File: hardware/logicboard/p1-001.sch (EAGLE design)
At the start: 70 parts, among them IC1 74LS06N, IC2 4066N, J1 MKR, J2 GPIO, J3 Vcc, J4 RLY, J42 RLY2, J5 SPI, J6 LED, J7 DIN5, J8 DIN5, J9 DIN5, K1 G5V1, Q1 220mA/50V/3.5Ω, Q2 220mA/50V/3.5Ω, T1 2SC1815, U1 DS18B20

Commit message: Removed many parts.
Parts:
- removed A, B: (no value), wirepad:SMD2
- removed C1: 22u, rcl:C-EU025-050X050
- removed C11, C4: 100n, rcl:C-EU025-024X044
- removed C12, C13, C3: 1u, rcl:C-EU050-024X044
- removed C2: 470n, rcl:C-EU050-024X044
- removed D1: DIODE-1N4148, SparkFun-DiscreteSemi:DIODE-1N4148
- removed F1: 1.8A, fuse:TE5
- removed H1, H2: STAND-OFF, SparkFun-Hardware:STAND-OFF
- removed IC1: 74LS06N, 74xx-us:74LS06N
- removed IC2: 4066N, 40xx:4066N
- removed J1: MKR, SparkFun-Connectors:CONN_05JST
- removed J2: GPIO, SparkFun-Connectors:CONN_03JST-PTH
- removed J3: Vcc, SparkFun-Connectors:CONN_02JST-PTH-2
- removed J4: RLY, SparkFun-Connectors:CONN_02-JST-2MM-SMT
- removed J5: SPI, SparkFun-Connectors:CONN_05JST-VERT
- removed J8, J9: DIN5, SparkFun-Connectors:DIN5
- removed JP1: PWRSEL, pinhead:PINHD-2X3
- removed JP2: RTC, SparkFun-Connectors:CONN_05
- removed JP4: RLYJMP, pinhead:PINHD-1X2
- removed JP5: PWR, pinhead:PINHD-1X3
- removed JP7: MNTR, pinhead:PINHD-1X4
- removed LCD1: AQM0802A-RN-GBW, AQM0802A-RN-GBW:AQM0802A-RN-GBW
- removed Q1, Q2: 220mA/50V/3.5Ω, SparkFun-DiscreteSemi:MOSFET-NCH-BSS138
- removed R101, R102, R103, R104: 10k, rcl:R-EU_M2012
- removed RN1: 10k, resistor-net:RN04
- removed RZ1**, RZ2**, VCCBRIDGE**: Inf, rcl:R-EU_M2012
- removed SV1: (no value), con-ml:ML16LE
- removed U1: DS18B20, SparkFun-Sensors:DS18B20
- removed V1: 5V, v-reg:78XXL
- removed VDDBRIDGE: 0, rcl:R-EU_M2012
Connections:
- removed net ANLG0R: IC2A.B, SV1-3.S
- removed net ANLG1R: IC2B.B, SV1-7.S
- removed net ANLG2R: IC2C.B, SV1-11.S
- removed net ANLG3R: IC2D.B, SV1-15.S
- removed net CAP1N: C12.2, LCD1.3
- removed net CAP1P: C12.1, LCD1.4
- removed net LCDVOUT: C13.2, LCD1.2
- removed net MO2RTN: RN4H.2
- removed net MO2SND: RN4G.2
- removed net MORTN: J9.5, RN4D.2
- removed net MOSND: J9.4, RN4C.2
- removed net MTRTN: J8.5, RN4F.2
- removed net MTSND: J8.4, RN4E.2
- removed net N$1: IC1D.O, RN4F.1
- removed net N$2: IC1E.O, RN4D.1
- removed net N$6: IC1F.O, RN4H.1
- removed net RLYOUT: J4.1, J42.1, K12.S
- removed net SCL: J1.3, Q1.D, R101.1, RZ1**.1
- removed net SDA3V: LCD1.7, Q2.S, R104.1, RZ2**.2
- removed net V+: C1.1, C2.1, D1.C, J0.3, JP1.1, JP5.3, V1.IN
- removed net VCC/VDD: C11.1, C13.1, LCD1.5, LCD1.9, VCCBRIDGE**.1, VDDBRIDGE.1
- removed net VOUT: F1.2, JP1.4, JP1.6
- removed net VOUTRAW: B.P, C3.1, C4.1, D1.A, J4.2, J42.2, JP4.2, K12.P, K12.P@1, V1.OUT
- removed net VOUTRAW2: A.P, F1.1, JP4.1, K12.O
- new net RLYOUT1: J42.1, K12.S
- new net RLYOUT2: J42.2, K12.P, K12.P@1
- net ANLG0: no longer IC2A.A, RN1.2
- net ANLG1: no longer IC2B.A, RN1.3
- net ANLG2: no longer IC2C.A, RN1.4
- net ANLG3: no longer IC2D.A, RN1.5
- net D7GATE: no longer IC2A.C, IC2B.C, IC2C.C, IC2D.C, J1.4
- net DTCT0: no longer SV1-2.S
- net DTCT1: no longer SV1-6.S
- net DTCT2: no longer SV1-10.S
- net DTCT3: no longer SV1-14.S
- net GND: no longer C1.2, C11.2, C2.2, C3.2, C4.2, IC2P.VSS, J1.1, J2.1, J3.1, J5.1, J8.2, J9.2, JP2.2, JP5.1, JP7.1, LCD1.6, RN1.1, SV1-1.S, SV1-13.S, SV1-5.S, SV1-9.S, U1.GND, V1.GND
- net GPIO0: no longer J2.2
- net GPIO1: no longer J2.3
- net MISO: no longer J5.5
- net MOSI: no longer J5.4
- net NMO2RTN: no longer IC1C.O, IC1F.I
- net NMORTN: no longer IC1B.O, IC1E.I
- net NMTRTN: no longer IC1A.O, IC1D.I
- net RX: no longer IC1A.I
- net SCK: no longer J5.3
- net SCL3V: no longer JP2.4, JP7.3, LCD1.8, Q1.S, R102.1, RZ1**.2
- net SDA: no longer J1.2, JP2.5, JP7.4, Q2.D, R103.1, RZ2**.1
- net THS: no longer U1.DQ
- net TX: no longer IC1B.I, IC1C.I
- net VCC: no longer IC2P.VDD, J1.5, J3.2, J5.2, JP1.3, JP2.1, JP5.2, JP7.2, R101.2, R103.2, RN4C.1, RN4E.1, RN4G.1, U1.VDD, VCCBRIDGE**.2
- net VCC/2: no longer JP1.5, SV1-12.S, SV1-16.S, SV1-4.S, SV1-8.S
- net VDD: no longer Q1.G, Q2.G, R102.2, R104.2, VDDBRIDGE.2
- net VIN: now also J0.3; no longer JP1.2

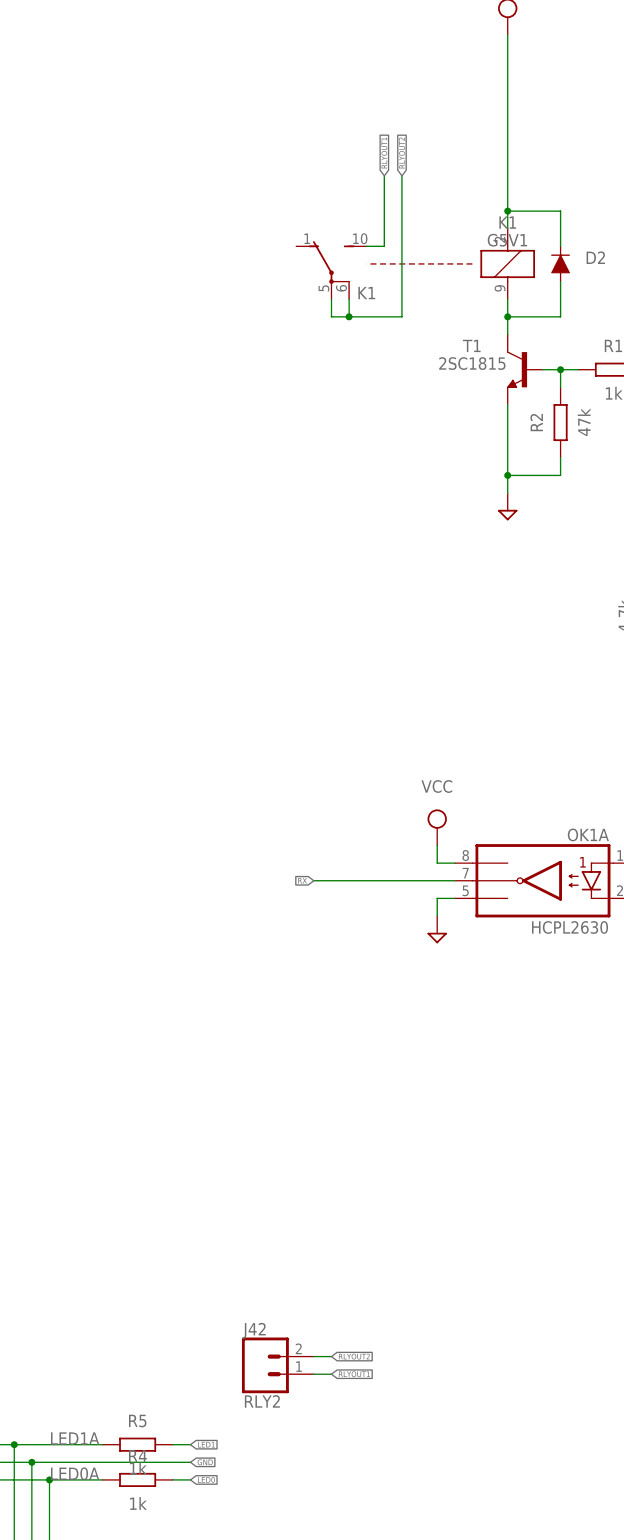
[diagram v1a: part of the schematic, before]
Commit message: 3-pin relay port.
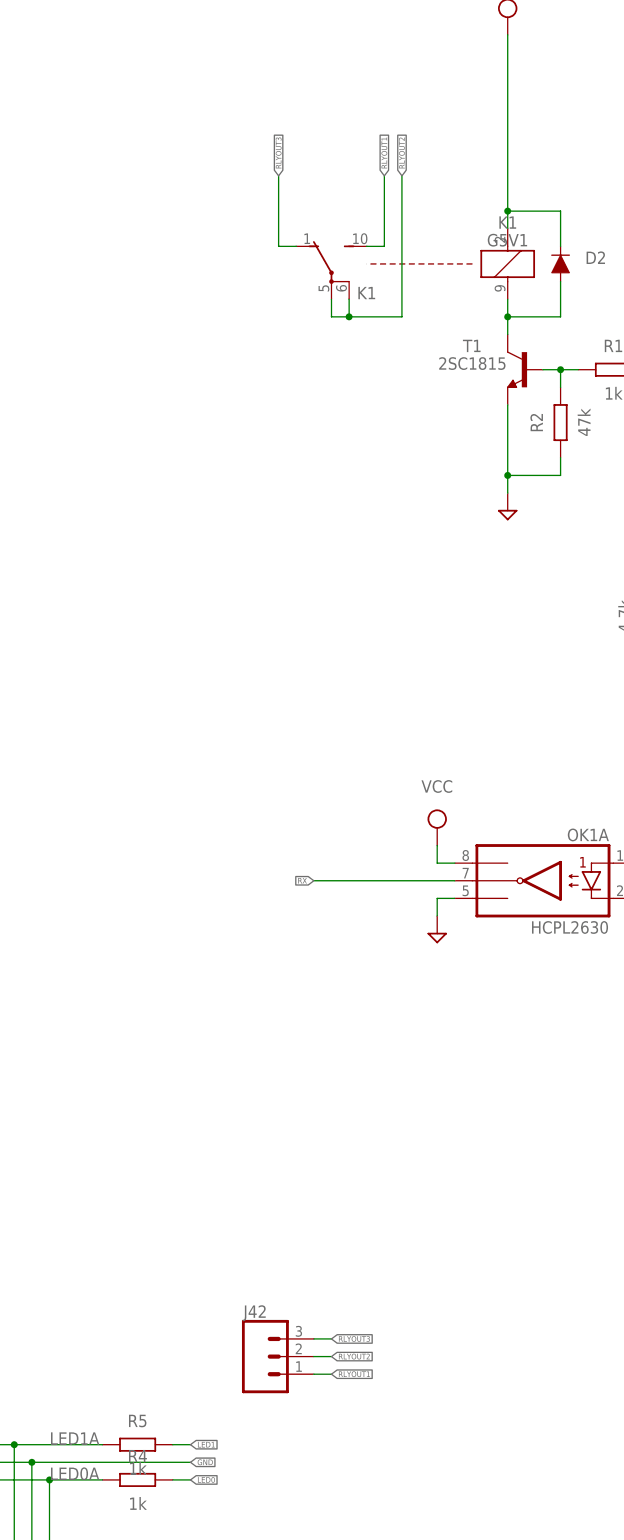
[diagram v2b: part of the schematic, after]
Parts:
- J42: value RLY2 -> (none); device SparkFun-Connectors:CONN_02JST-PTH-2 -> SparkFun-Connectors:CONN_03JST-PTH
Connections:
- new net RLYOUT3: J42.3, K12.O
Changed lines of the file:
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@@
 <part name="SUPPLY24" library="supply2" library_urn="urn:adsk.eagle:library:372" deviceset="VCC" device=""/>
 <part name="SUPPLY25" library="supply2" library_urn="urn:adsk.eagle:library:372" deviceset="VCC" device=""/>
-<part name="J42" library="SparkFun-Connectors" library_urn="urn:adsk.eagle:library:513" deviceset="CONN_02" device="JST-PTH-2" package3d_urn="urn:adsk.eagle:package:38053/1" value="RLY2"/>
+<part name="J42" library="SparkFun-Connectors" library_urn="urn:adsk.eagle:library:513" deviceset="CONN_03" device="JST-PTH" package3d_urn="urn:adsk.eagle:package:38069/1"/>
 </parts>
 <sheets>
@@
 <attribute name="VALUE" x="312.42" y="119.38" size="1.778" layer="96" align="bottom-center"/>
 </instance>
-<instance part="J42" gate="G$1" x="111.76" y="48.26" smashed="yes">
+<instance part="J42" gate="J$1" x="111.76" y="50.8" smashed="yes">
 <attribute name="VALUE" x="109.22" y="43.434" size="1.778" layer="96" font="vector"/>
-<attribute name="NAME" x="109.22" y="53.848" size="1.778" layer="95" font="vector"/>
+<attribute name="NAME" x="109.22" y="56.388" size="1.778" layer="95" font="vector"/>
 </instance>
 </instances>
@@
 <wire x1="119.38" y1="48.26" x2="121.92" y2="48.26" width="0.1524" layer="91"/>
 <label x="121.92" y="48.26" size="0.8128" layer="95" xref="yes"/>
-<pinref part="J42" gate="G$1" pin="1"/>
+<pinref part="J42" gate="J$1" pin="1"/>
 </segment>
 </net>
@@
 <wire x1="119.38" y1="50.8" x2="121.92" y2="50.8" width="0.1524" layer="91"/>
 <label x="121.92" y="50.8" size="0.8128" layer="95" xref="yes"/>
-<pinref part="J42" gate="G$1" pin="2"/>
+<pinref part="J42" gate="J$1" pin="2"/>
 </segment>
 </net>
@@
 </segment>
 </net>
+<net name="RLYOUT3" class="0">
+<segment>
+<pinref part="K1" gate="2" pin="O"/>
+<wire x1="116.84" y1="210.82" x2="114.3" y2="210.82" width="0.1524" layer="91"/>
+<wire x1="114.3" y1="210.82" x2="114.3" y2="220.98" width="0.1524" layer="91"/>
+<label x="114.3" y="220.98" size="0.8128" layer="95" rot="R90" xref="yes"/>
+</segment>
+<segment>
+<pinref part="J42" gate="J$1" pin="3"/>
+<wire x1="119.38" y1="53.34" x2="121.92" y2="53.34" width="0.1524" layer="91"/>
+<label x="121.92" y="53.34" size="0.8128" layer="95" xref="yes"/>
+</segment>
+</net>

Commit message: Removed many parts.
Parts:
- removed J6: LED, SparkFun-Connectors:CONN_03JST-PTH-VERT
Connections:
- net GND: no longer J6.2
- net LED0A: no longer J6.3
- net LED1A: no longer J6.1
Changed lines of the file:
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@@
 <part name="SUPPLY6" library="supply2" deviceset="GND" device=""/>
 <part name="C9" library="resistor" library_urn="urn:adsk.eagle:library:348" deviceset="C-EU" device="025-024X044" package3d_urn="urn:adsk.eagle:package:23630/1" value="100n"/>
-<part name="J6" library="SparkFun-Connectors" library_urn="urn:adsk.eagle:library:513" deviceset="CONN_03" device="JST-PTH-VERT" package3d_urn="urn:adsk.eagle:package:38080/1" value="LED"/>
 <part name="SV3" library="pinhead" library_urn="urn:adsk.eagle:library:325" deviceset="PINHD-2X7" device="" package3d_urn="urn:adsk.eagle:package:22478/2" value="Testport II"/>
 <part name="SUPPLY9" library="supply2" library_urn="urn:adsk.eagle:library:372" deviceset="VCC" device=""/>
@@
 <attribute name="VALUE" x="289.56" y="208.28" size="1.778" layer="96" align="bottom-center"/>
 </instance>
-<instance part="J6" gate="J$1" x="66.04" y="20.32" smashed="yes">
-<attribute name="VALUE" x="63.5" y="12.954" size="1.778" layer="96" font="vector"/>
-<attribute name="NAME" x="63.5" y="25.908" size="1.778" layer="95" font="vector"/>
-</instance>
 <instance part="SV3" gate="A" x="327.66" y="195.58" smashed="yes">
 <attribute name="NAME" x="321.31" y="206.375" size="1.778" layer="95"/>
@@
 <segment>
 <label x="101.6" y="35.56" size="0.8128" layer="95" xref="yes"/>
-<wire x1="66.04" y1="35.56" x2="78.74" y2="35.56" width="0.1524" layer="91"/>
 <pinref part="JP6" gate="A" pin="2"/>
-<pinref part="J6" gate="J$1" pin="2"/>
-<wire x1="78.74" y1="35.56" x2="101.6" y2="35.56" width="0.1524" layer="91"/>
-<wire x1="73.66" y1="20.32" x2="78.74" y2="20.32" width="0.1524" layer="91"/>
-<wire x1="78.74" y1="20.32" x2="78.74" y2="35.56" width="0.1524" layer="91"/>
-<junction x="78.74" y="35.56"/>
+<wire x1="66.04" y1="35.56" x2="101.6" y2="35.56" width="0.1524" layer="91"/>
 </segment>
 <segment>
@@
 <net name="LED1A" class="0">
 <segment>
-<wire x1="88.9" y1="38.1" x2="76.2" y2="38.1" width="0.1524" layer="91"/>
+<wire x1="88.9" y1="38.1" x2="66.04" y2="38.1" width="0.1524" layer="91"/>
 <label x="81.28" y="38.1" size="1.778" layer="95"/>
 <pinref part="R5" gate="G$1" pin="1"/>
 <pinref part="JP6" gate="A" pin="1"/>
-<pinref part="J6" gate="J$1" pin="1"/>
-<wire x1="76.2" y1="38.1" x2="66.04" y2="38.1" width="0.1524" layer="91"/>
-<wire x1="73.66" y1="17.78" x2="76.2" y2="17.78" width="0.1524" layer="91"/>
-<wire x1="76.2" y1="17.78" x2="76.2" y2="38.1" width="0.1524" layer="91"/>
-<junction x="76.2" y="38.1"/>
 </segment>
 </net>
@@
 <net name="LED0A" class="0">
 <segment>
-<wire x1="88.9" y1="33.02" x2="81.28" y2="33.02" width="0.1524" layer="91"/>
 <label x="81.28" y="33.02" size="1.778" layer="95"/>
 <pinref part="R4" gate="G$1" pin="1"/>
 <pinref part="JP6" gate="A" pin="3"/>
-<pinref part="J6" gate="J$1" pin="3"/>
-<wire x1="81.28" y1="33.02" x2="66.04" y2="33.02" width="0.1524" layer="91"/>
-<wire x1="73.66" y1="22.86" x2="81.28" y2="22.86" width="0.1524" layer="91"/>
-<wire x1="81.28" y1="22.86" x2="81.28" y2="33.02" width="0.1524" layer="91"/>
-<junction x="81.28" y="33.02"/>
-</segment>
-</net>
+<wire x1="88.9" y1="33.02" x2="66.04" y2="33.02" width="0.1524" layer="91"/>
+</segment>
+</net>

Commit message: Removed several parts.
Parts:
- removed C10: 100n, rcl:C-EU025-024X044
- removed R3: 1k, resistor:R-EU_0204/5
- removed RN2, RN3: 4.7k, resistor-net:RN04
- removed RN4: 220, resistor-dil:8R-N
- added RA: 220, resistor:R-EU_0204/5
- added RB: 4.7k, resistor:R-EU_0204/5
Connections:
- removed net MNTRA: OK1B.A2, RN4A.2
- removed net NMO2RTN: RN2.5
- removed net NMORTN: RN2.4
- removed net NMTRTN: RN2.3
- removed net SCL3V: MC1.3, RN3.3, SV3.9
- removed net VCC/2: R3.2, RN4A.1
- new net SCL: MC1.3, SV3.9
- net AREF: no longer C10.1, R3.1
- net GND: now also OK1B.A2; no longer C10.2
- net MIDIINSND: now also RA.1; no longer RN4B.1
- net MISND: now also RA.2; no longer RN4B.2
- net MNTR: no longer RN3.5
- net RX: now also RB.1; no longer RN2.2
- net SDA: no longer RN3.2
- net THS: no longer RN3.4
- net VCC: now also RB.2; no longer RN2.1, RN3.1

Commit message: Removed many parts.
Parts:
- renumbered J42 to J4

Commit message: The first should-be-working model.
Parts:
- added D2B, D2C: DIODE-1N4148, SparkFun-DiscreteSemi:DIODE-1N4148
- added J4B, J4C: (no value), SparkFun-Connectors:CONN_03JST-PTH
- added K1B, K1C: G5V1, relay:G5V1
- added R1B, R1C: 1k, resistor:R-EU_0204/5
- added R2B, R2C: 47k, resistor:R-EU_0204/5
- added T1B, T1C: 2SC1815, transistor:2SC1815
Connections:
- new net RLYDRV1: R1B.1, R2B.2, T1B.B
- new net RLYDRV2: R1C.1, R2C.2, T1C.B
- new net RLYOUT1B: J4B.1, K1B2.S
- new net RLYOUT1C: J4C.1, K1C2.S
- new net RLYOUT2B: J4B.2, K1B2.P, K1B2.P@1
- new net RLYOUT2C: J4C.2, K1C2.P, K1C2.P@1
- new net RLYOUT3A: J4B.3
- new net RLYOUT3B: K1B2.O
- new net RLYOUT3C: J4C.3, K1C2.O
- new net RLYSNK1: D2B.A, K1B1.2, T1B.C
- new net RLYSNK2: D2C.A, K1C1.2, T1C.C
- net GND: now also R2B.1, R2C.1, T1B.E, T1C.E
- net GPIO0: now also R1B.2
- net GPIO1: now also R1C.2
- net VCC: now also D2B.C, D2C.C, K1B1.1, K1C1.1
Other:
- moved on the sheet: D2, J0, K1, R1, R2, T1

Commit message: Silk.
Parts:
- removed RA: 220, resistor:R-EU_0204/5
- removed RB: 4.7k, resistor:R-EU_0204/5
- added R1A: 1k, resistor:R-EU_0204/5
- added R2A: 47k, resistor:R-EU_0204/5
- R1: value 1k -> 220
- R2: value 47k -> 4.7k
- renumbered C7 to C7A, C8 to C7B, C9 to C7C, D2 to D2A, J4 to J4A, K1 to K1A, T1 to T1A
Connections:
- net GND: now also R2A.1; no longer R2.1
- net MIDIINSND: now also R1.1; no longer RA.1
- net MISND: now also R1.2; no longer RA.2
- net RLY: now also R1A.2; no longer R1.2
- net RLYDRV: now also R1A.1, R2A.2; no longer R1.1, R2.2
- net RX: now also R2.1; no longer RB.1
- net VCC: now also R2.2; no longer RB.2
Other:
- moved on the sheet: R1, R2
